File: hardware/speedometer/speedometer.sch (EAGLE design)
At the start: 128 parts, among them IC1 PIC32MX274F256DT-I_PT, IC10 TPS63001DRCT, IC11 TPS63002DRCT, IC2 CSTCE8M00G55-R0, IC3 HM-11, IC4 BQ27441DRZR-G1A, IC5 BQ24075RGTT, IC6 NRF24L01P-T, IC7 CSTCE16M0V53-R0, IC8 24LC024SN, IC9 MAX16054AZT+T, J1 10104111-0001LF, J2 BAT, J3 CONUFL001-SMD-T, J4 Right_sens, J5 Right, J6 Left_sens, J7 Left, Q1 BC817, Q2 BC817, Q3 BC817, Q4 BC817, U1 SN74AHC1G08DBVR, U2 SN74AHC1G08DBVR

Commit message: wip, mostly done
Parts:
- removed JP1, JP2: (no value), pinhead:PINHD-1X2
- added X1, X2: TSW-102-07-G-S, con-samtec:TSW-102-07-G-S
- SV1: device con-lsta:FE06-1 -> con-lstb:MA03-2
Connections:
- net +3V3: now also X2-1.1; no longer JP2.1
- net BL_TRIG: now also X2-2.1; no longer JP2.2
- net GND: now also X1-2.1; no longer JP1.2
- net N$41: now also X1-1.1; no longer JP1.1

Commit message: power added
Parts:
- C10, C21, C22, C25, C26, C27, C28: device rcl:C-EUC0603K -> rcl:C-EUC0805K
- C11: value 100n -> 10u; device rcl:C-EUC0603K -> rcl:C-EUC0805K
- C12: value 4u7 -> 10u; device rcl:CPOL-EUSMCA -> rcl:C-EUC0805K
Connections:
- net BQ_1V8: no longer R12.1
- net GND: now also C12.2, R12.1; no longer C12.-
- net VCCINT: now also C12.1; no longer C12.+
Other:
- moved on the sheet: C8, J2

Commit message: wip
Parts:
- C3: device rcl:C-EUC0603K -> rcl:C-EUC0805K
- SV1: device con-lstb:MA03-2 -> con-lstb:MA06-1
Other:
- moved on the sheet: SV1
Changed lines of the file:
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@@
 <part name="GND11" library="supply1" library_urn="urn:adsk.eagle:library:371" deviceset="GND" device=""/>
 <part name="VDD1" library="supply1" library_urn="urn:adsk.eagle:library:371" deviceset="VDD" device=""/>
-<part name="C3" library="rcl" library_urn="urn:adsk.eagle:library:334" deviceset="C-EU" device="C0603K" value="10u"/>
+<part name="C3" library="rcl" library_urn="urn:adsk.eagle:library:334" deviceset="C-EU" device="C0805K" package3d_urn="urn:adsk.eagle:package:23681/2" value="10u"/>
 <part name="GND2" library="supply1" library_urn="urn:adsk.eagle:library:371" deviceset="GND" device=""/>
 <part name="C1" library="rcl" library_urn="urn:adsk.eagle:library:334" deviceset="C-EU" device="C0603K" value="100n"/>
@@
 <part name="GND63" library="supply1" library_urn="urn:adsk.eagle:library:371" deviceset="GND" device=""/>
 <part name="+3V2" library="supply1" library_urn="urn:adsk.eagle:library:371" deviceset="+3V3" device=""/>
-<part name="SV1" library="con-lstb" library_urn="urn:adsk.eagle:library:162" deviceset="MA03-2" device="" package3d_urn="urn:adsk.eagle:package:8334/1"/>
 <part name="X1" library="con-samtec" library_urn="urn:adsk.eagle:library:184" deviceset="TSW-102-*-G-S" device="" technology="07"/>
 <part name="X2" library="con-samtec" library_urn="urn:adsk.eagle:library:184" deviceset="TSW-102-*-G-S" device="" technology="07"/>
 <part name="GND64" library="supply1" library_urn="urn:adsk.eagle:library:371" deviceset="GND" device=""/>
+<part name="SV1" library="con-lstb" library_urn="urn:adsk.eagle:library:162" deviceset="MA06-1" device="" package3d_urn="urn:adsk.eagle:package:8340/1"/>
 </parts>
 <sheets>
@@
 <attribute name="SHEET" x="230.505" y="5.08" size="2.54" layer="94"/>
 </instance>
-<instance part="GND1" gate="1" x="40.64" y="149.86" smashed="yes">
-<attribute name="VALUE" x="38.1" y="147.32" size="1.778" layer="96"/>
-</instance>
-<instance part="+3V34" gate="G$1" x="7.62" y="167.64" smashed="yes" rot="R90">
-<attribute name="VALUE" x="12.7" y="165.1" size="1.778" layer="96" rot="R180"/>
+<instance part="GND1" gate="1" x="27.94" y="149.86" smashed="yes">
+<attribute name="VALUE" x="25.4" y="147.32" size="1.778" layer="96"/>
+</instance>
+<instance part="+3V34" gate="G$1" x="50.8" y="165.1" smashed="yes" rot="R270">
+<attribute name="VALUE" x="45.72" y="167.64" size="1.778" layer="96"/>
 </instance>
 <instance part="TP8" gate="G$1" x="236.22" y="139.7" smashed="yes">
@@
 <attribute name="VALUE" x="34.29" y="50.038" size="1.778" layer="96"/>
 </instance>
-<instance part="SV1" gate="1" x="30.48" y="160.02" smashed="yes" rot="MR180">
-<attribute name="VALUE" x="26.67" y="167.64" size="1.778" layer="96" rot="MR180"/>
-<attribute name="NAME" x="26.67" y="154.178" size="1.778" layer="95" rot="MR180"/>
-</instance>
 <instance part="X1" gate="-1" x="95.25" y="142.24" smashed="yes">
 <attribute name="VALUE" x="93.98" y="143.51" size="1.778" layer="96"/>
@@
 <instance part="X2" gate="-2" x="110.49" y="27.94" smashed="yes">
 <attribute name="NAME" x="113.03" y="27.178" size="1.524" layer="95"/>
+</instance>
+<instance part="SV1" gate="1" x="15.24" y="160.02" smashed="yes" rot="MR180">
+<attribute name="VALUE" x="13.97" y="172.72" size="1.778" layer="96" rot="MR180"/>
+<attribute name="NAME" x="13.97" y="151.638" size="1.778" layer="95" rot="MR180"/>
 </instance>
 </instances>
@@
 <segment>
 <pinref part="SV1" gate="1" pin="3"/>
-<wire x1="38.1" y1="160.02" x2="40.64" y2="160.02" width="0.1524" layer="91"/>
+<wire x1="22.86" y1="162.56" x2="27.94" y2="162.56" width="0.1524" layer="91"/>
 <pinref part="GND1" gate="1" pin="GND"/>
-<wire x1="40.64" y1="160.02" x2="40.64" y2="152.4" width="0.1524" layer="91"/>
+<wire x1="27.94" y1="162.56" x2="27.94" y2="152.4" width="0.1524" layer="91"/>
 </segment>
 </net>
@@
 </segment>
 <segment>
+<pinref part="SV1" gate="1" pin="2"/>
 <pinref part="+3V34" gate="G$1" pin="+3V3"/>
-<wire x1="10.16" y1="167.64" x2="15.24" y2="167.64" width="0.1524" layer="91"/>
-<wire x1="15.24" y1="167.64" x2="15.24" y2="162.56" width="0.1524" layer="91"/>
-<pinref part="SV1" gate="1" pin="2"/>
-<wire x1="15.24" y1="162.56" x2="22.86" y2="162.56" width="0.1524" layer="91"/>
+<wire x1="22.86" y1="165.1" x2="48.26" y2="165.1" width="0.1524" layer="91"/>
 </segment>
 </net>
@@
 <segment>
 <pinref part="SV1" gate="1" pin="5"/>
-<wire x1="38.1" y1="157.48" x2="45.72" y2="157.48" width="0.1524" layer="91"/>
-<label x="45.72" y="157.48" size="1.27" layer="95" font="vector" xref="yes"/>
+<wire x1="22.86" y1="157.48" x2="33.02" y2="157.48" width="0.1524" layer="91"/>
+<wire x1="33.02" y1="157.48" x2="33.02" y2="154.94" width="0.1524" layer="91"/>
+<wire x1="33.02" y1="154.94" x2="35.56" y2="154.94" width="0.1524" layer="91"/>
+<label x="35.56" y="154.94" size="1.778" layer="95" font="vector" xref="yes"/>
 </segment>
 </net>
@@
 <segment>
 <pinref part="SV1" gate="1" pin="4"/>
-<wire x1="22.86" y1="160.02" x2="15.24" y2="160.02" width="0.1524" layer="91"/>
-<label x="15.24" y="160.02" size="1.27" layer="95" font="vector" rot="R180" xref="yes"/>
+<wire x1="22.86" y1="160.02" x2="35.56" y2="160.02" width="0.1524" layer="91"/>
+<label x="35.56" y="160.02" size="1.778" layer="95" font="vector" xref="yes"/>
 </segment>
 </net>
@@
 <segment>
 <pinref part="SV1" gate="1" pin="1"/>
-<wire x1="38.1" y1="162.56" x2="45.72" y2="162.56" width="0.1524" layer="91"/>
-<label x="45.72" y="162.56" size="1.27" layer="95" font="vector" xref="yes"/>
-</segment>
-</net>
+<wire x1="22.86" y1="167.64" x2="35.56" y2="167.64" width="0.1524" layer="91"/>
+<label x="35.56" y="167.64" size="1.778" layer="95" font="vector" xref="yes"/>
+</segment>
+</net>

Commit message: wip
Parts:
- added IC12: SN65220DBVRG4, SN65220DBVRG4:SN65220DBVRG4
- IC8: value 24LC024SN -> 24LC024ST; device microchip:24LC024SN -> microchip:24LC024ST
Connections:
- net GND: now also IC12.GND
- net USB_D+: now also IC12.A
- net USB_D-: now also IC12.B
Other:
- moved on the sheet: C6, J1, R2, R3, TP1, TP2, X1-1, X1-2

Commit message: wip
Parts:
- added C30, C31, C32: (no value), rcl:C-EUC0402K
- added R36, R37, R38: 0, rcl:R-US_R0402
- added U$1: M310210, m310210:M310210
- C18: value 1p5 -> (none)
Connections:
- new net N$17: C19.1, L2.P$1, R36.2
- new net N$20: C18.2, C30.1, R37.1, R38.1
- new net N$23: J3.SIG, R37.2
- new net N$36: C32.1, U$1.GND
- net GND: now also C30.2, C31.2, C32.2
- net N$32: now also R36.1; no longer L2.P$1
- net N$37: now also C31.1, R38.2, U$1.FEED; no longer C18.2, C19.1, J3.SIG
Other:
- moved on the sheet: C15, C16, C17, C18, C19, IC6, IC7, J3, L1, L2, L3, R19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

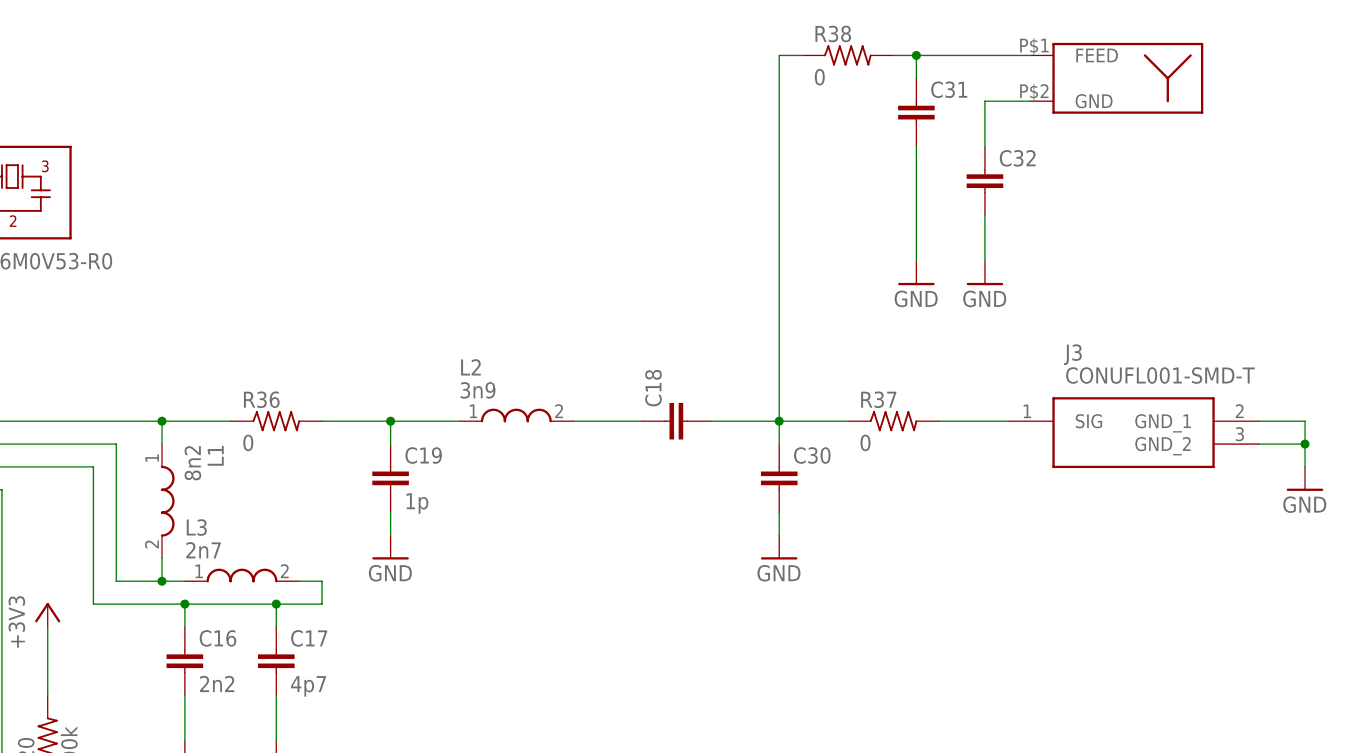
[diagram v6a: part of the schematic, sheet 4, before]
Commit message: aligned with GF suggestion, waiting approval
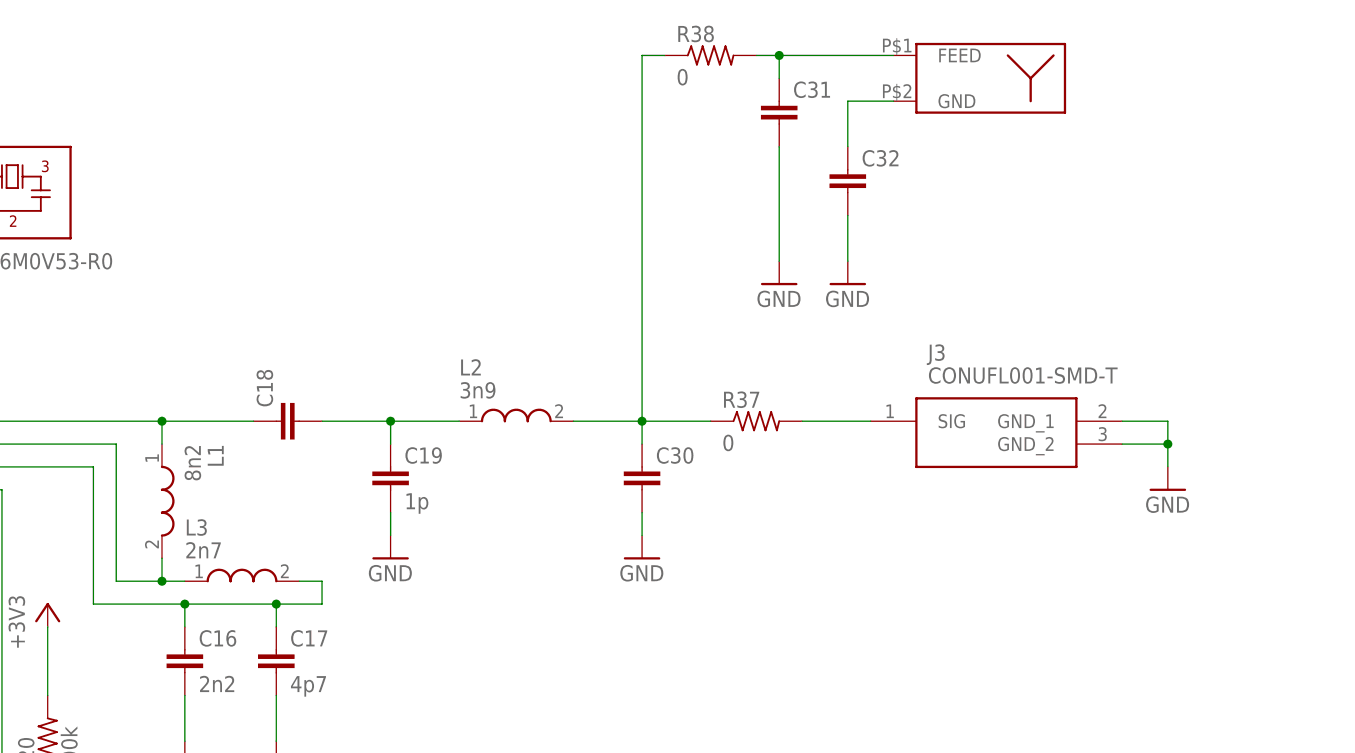
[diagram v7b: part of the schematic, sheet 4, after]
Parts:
- removed R10: 470, rcl:R-US_R0603
- removed R36: 0, rcl:R-US_R0402
- added TP25, TP26: TPB1,27, testpad:TPB1,27
- added U$2: 74LVC1G32SE-7, 74LVC1G32SE:74LVC1G32SE-7
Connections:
- removed net BT_KEY: IC1.RPC5/PMD7/RC5, R10.2
- removed net N$18: C18.1, L2.P$2
- new net KEEP_SYS_EN: IC1.RPC5/PMD7/RC5, TP26.TP, U$2.B
- new net MAX_SYS_ON: IC9.OUT, TP25.TP, U$2.A
- net GND: now also U$2.GND
- net N$17: now also C18.2; no longer R36.2
- net N$2: no longer R10.1
- net N$20: now also L2.P$2; no longer C18.2
- net N$32: now also C18.1; no longer R36.1
- net SYS_EN: now also U$2.Y; no longer IC9.OUT
- net VCCINT: now also U$2.VCC
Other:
- moved on the sheet: C18, C30, C31, C32, IC9, J3, R37, R38, S1, TP20

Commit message: part renumber
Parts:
- removed CHG, STATUS: (no value), led:LED3MM
- removed R37, R38: 0, rcl:R-US_R0402
- added LED5, LED6: (no value), led:LEDCHIPLED_1206
- added R10: 470, rcl:R-US_R0603
- added R36: 1k5, rcl:R-US_R0603
- C15: value 33n -> 1n; device rcl:C-EUC0402K -> rcl:C-EUC0603K
- C16: value 2n2 -> 33n
- C17: value 4p7 -> 2n2
- C19: value 1p -> 4p7
- C20: value 100n -> 1p; device rcl:C-EUC0603K -> rcl:C-EUC0402K
- C21, C22: value 10u -> (none); device rcl:C-EUC0805K -> rcl:C-EUC0402K
- C23: value 100n -> (none); device rcl:C-EUC0603K -> rcl:C-EUC0402K
- C27, C28: value 10u -> 100n; device rcl:C-EUC0805K -> rcl:C-EUC0603K
- C29: value 1n -> 10u; device rcl:C-EUC0603K -> rcl:C-EUC0805K
- C30, C31, C32: value (none) -> 10u; device rcl:C-EUC0402K -> rcl:C-EUC0805K
- IC10: value TPS63001DRCT -> MAX16054AZT+T; device TPS63000DRCT:TPS63000DRCT -> MAX16054AZT+T:MAX16054AZT+T
- IC11: value TPS63002DRCT -> TPS63001DRCT
- IC12: value SN65220DBVRG4 -> TPS63002DRCT; device SN65220DBVRG4:SN65220DBVRG4 -> TPS63000DRCT:TPS63000DRCT
- IC2: value CSTCE8M00G55-R0 -> SN65220DBVRG4; device CSTCE12M0G15L99-R0:CSTCE12M0G15L99-R0 -> SN65220DBVRG4:SN65220DBVRG4
- IC3: value HM-11 -> CSTCE8M00G55-R0; device HM11:HM-11 -> CSTCE12M0G15L99-R0:CSTCE12M0G15L99-R0
- IC4: value BQ27441DRZR-G1A -> HM-11; device BQ27441DRZR-G1A:BQ27441DRZR-G1A -> HM11:HM-11
- IC5: value BQ24075RGTT -> BQ27441DRZR-G1A; device BQ24075RGTT:BQ24075RGTT -> BQ27441DRZR-G1A:BQ27441DRZR-G1A
- IC6: value NRF24L01P-T -> BQ24075RGTT; device nRF24L01P-T:NRF24L01P-T -> BQ24075RGTT:BQ24075RGTT
- IC7: value CSTCE16M0V53-R0 -> NRF24L01P-T; device CSTCE12M0G15L99-R0:CSTCE12M0G15L99-R0 -> nRF24L01P-T:NRF24L01P-T
- IC8: value 24LC024ST -> CSTCE16M0V53-R0; device microchip:24LC024ST -> CSTCE12M0G15L99-R0:CSTCE12M0G15L99-R0
- IC9: value MAX16054AZT+T -> 24LC024ST; device MAX16054AZT+T:MAX16054AZT+T -> microchip:24LC024ST
- L2: value 3n9 -> 2n7
- L3: value 2n7 -> 3n9
- LED1: device led:LEDCHIPLED_0805 -> led:LED3MM
- LED2: device led:LEDCHIPLED_1206 -> led:LEDCHIPLED_0805
- LED4: device led:LEDCHIPLED_1206 -> led:LED3MM
- R2: value 1k -> 1k5
- R21, R22: value 100 -> 0; device rcl:R-US_R0603 -> rcl:R-US_R0402; RS_PART_NUMBER 740-8978 -> (none)
- R23, R24: value 10k -> 100; RS_PART_NUMBER (none) -> 740-8978
- R25: value 100k -> 10k
- R28, R32, R35: value 1k5 -> 10k
- R29, R34: value 10k -> 100k
- R3: value 10k -> 1k
- R30: value 100k -> 1k5
- R5: value 4k7 -> 10k
- R8: value 470 -> 4k7
- TP20: TP_SIGNAL_NAME TP_SYS_EN -> TP_SYS_EN_PIC
- TP21: TP_SIGNAL_NAME TP_3V3 -> TP_SYS_EN_MAX
- TP22: TP_SIGNAL_NAME TP_5V -> TP_3V3
- TP23: TP_SIGNAL_NAME TP_L_DX -> TP_5V
- TP24: TP_SIGNAL_NAME TP_L_DX -> TP_SYS_EN
- TP25: TP_SIGNAL_NAME TP_SYS_EN_MAX -> TP_L_DX
- TP26: TP_SIGNAL_NAME TP_SYS_EN_PIC -> TP_L_DX
- renumbered BT to LED3, JP3 to JP1, U$1 to ANT1, U$2 to IC13
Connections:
- removed net N$10 (its old number): R35.1, STATUS.C
- new net N$29: LED2.C, R2.1
- net !BAT_CHG: now also IC6.!CHG, LED4.C; no longer CHG.C, IC5.!CHG
- net !MCLR: now also R3.1; no longer R2.1
- net +3V3: now also C15.1, C24.1, C31.1, IC11.FB, IC11.VOUT, IC4.VCC, IC6.EN1, IC7.VDD_1, IC7.VDD_2, IC7.VDD_3, IC9.VCC, R28.2, R35.2, R4.2, R8.2, TP22.TP; no longer C20.1, C25.1, C27.1, IC10.FB, IC10.VOUT, IC3.VCC, IC5.EN1, IC6.VDD_1, IC6.VDD_2, IC6.VDD_3, IC8.VCC, R26.2, R3.2, R34.2, R5.2, TP21.TP
- net +5V: now also C30.1, C32.1, IC12.FB, IC12.VOUT, LED5.A, LED6.A, TP23.TP; no longer C26.1, C28.1, IC11.FB, IC11.VOUT, LED2.A, LED4.A, TP22.TP
- net BL_TRIG: now also R5.2; no longer R4.2
- net BQ_1V8: now also IC5.VDD; no longer IC4.VDD
- net BQ_PGOOD: now also IC6.!PGOOD; no longer IC5.!PGOOD
- net BT_RST: now also R9.1; no longer R7.1
- net GAUGE_GP: now also IC5.GPOUT; no longer IC4.GPOUT
- net GND: now also IC10.CLEAR, IC12.PGND, IC2.GND, IC3.2, IC4.GND, IC5.EP, IC6.!CE, IC6.EN2, IC6.SYSOFF, IC6.VSS, IC6.VSS_TP, IC7.TP_GND, IC7.VSS_1, IC7.VSS_2, IC7.VSS_3, IC7.VSS_4, IC8.2, IC9.A0, IC9.A1, IC9.A2, IC9.WP, R2.2, R29.2, R34.2, R5.1; no longer IC10.PGND, IC2.2, IC3.GND, IC4.EP, IC4.VSS, IC5.!CE, IC5.EN2, IC5.SYSOFF, IC5.VSS_TP, IC6.TP_GND, IC6.VSS_1, IC6.VSS_2, IC6.VSS_3, IC6.VSS_4, IC7.2, IC8.A0, IC8.A1, IC8.A2, IC8.GND, IC8.WP, IC9.CLEAR, R25.2, R30.2, R35.2, R4.1
- net I2C2_SCL: now also IC5.SCL, IC9.SCL, R7.1; no longer IC4.SCL, IC8.SCL, R6.1
- net I2C2_SDA: now also IC5.SDA, IC9.SDA, R6.1; no longer IC4.SDA, IC8.SDA, R5.1
- net IN_L: now also R35.1; no longer R34.1
- net IN_R: now also R28.1; no longer R26.1
- net KEEP_SYS_EN: now also TP20.TP; no longer TP26.TP
- net LED_HB: now also LED2.A; no longer LED1.A
- net LED_STS: now also LED1.A; no longer STATUS.A
- net MAX_SYS_ON: now also IC10.OUT, TP21.TP; no longer IC9.OUT, TP25.TP
- net N$1: now also IC4.!RESET, R9.2; no longer IC3.!RESET, R8.2
- net N$11: now also IC3.1; no longer IC2.1
- net N$12: now also LED4.A; no longer CHG.A
- net N$13: now also R32.2, R34.1; no longer R31.2, R33.1
- net N$14: now also R31.2, R33.1, TP26.TP; no longer R29.2, R30.1, TP24.TP
- net N$15: now also LED6.C, R36.2; no longer LED2.C, R32.2
- net N$16: now also R31.1; no longer R29.1
- net N$17: now also C20.1, L3.P$1; no longer C19.1, L2.P$1
- net N$19: now also IC3.3; no longer IC2.3
- net N$2: now also IC4.PIO0/KEY; no longer IC3.PIO0/KEY
- net N$20: now also C21.1, L3.P$2, R21.1, R22.1; no longer C30.1, L2.P$2, R37.1, R38.1
- net N$22: now also IC7.XC2, IC8.1; no longer IC6.XC2, IC7.1
- net N$23: now also R22.2; no longer R37.2
- net N$24: now also IC7.IREF; no longer IC6.IREF
- net N$25: now also C16.1, IC7.DVDD; no longer C15.1, IC6.DVDD
- net N$26: now also R25.2, R27.1; no longer R23.2, R25.1
- net N$27: now also R25.1; no longer R23.1
- net N$28: now also R32.1; no longer R31.1
- net N$3: now also R36.1; no longer R32.1
- net N$30: now also IC5.BIN; no longer IC4.BIN
- net N$31: now also IC7.XC1, IC8.3; no longer IC6.XC1, IC7.3
- net N$32: now also IC7.ANT2; no longer IC6.ANT2
- net N$33: now also IC7.ANT1, L2.P$1; no longer IC6.ANT1, L3.P$1
- net N$34: now also IC11.L2; no longer IC10.L2
- net N$35: now also C19.1, IC7.VDD_PA, L2.P$2; no longer C16.1, IC6.VDD_PA, L3.P$2
- net N$36: now also C23.1; no longer C32.1
- net N$37: now also C22.1, R21.2; no longer C31.1, R38.2
- net N$38: now also R30.1; no longer R28.1
- net N$39: now also R26.2, R29.1, TP25.TP; no longer R24.2, R27.1, TP23.TP
- net N$4: now also IC4.PIO1/LED, R10.1; no longer IC3.PIO1/LED, R9.1
- net N$40: now also LED5.C, R30.2; no longer LED4.C, R28.2
- net N$41: now also R3.2, R4.1; no longer R2.2, R3.1
- net N$42: now also R26.1; no longer R24.1
- net N$5: now also IC11.L1; no longer IC10.L1
- net N$58: now also IC10.IN; no longer IC9.IN
- net N$59: now also IC12.L1; no longer IC11.L1
- net N$6: now also R10.2; no longer R9.2
- net N$60: now also C27.1, IC11.PS/SYNC, IC11.VINA, R23.1; no longer C23.1, IC10.PS/SYNC, IC10.VINA, R21.1
- net N$61: now also IC12.L2; no longer IC11.L2
- net N$62: now also C28.1, IC12.PS/SYNC, IC12.VINA, R24.1; no longer C24.1, IC11.PS/SYNC, IC11.VINA, R22.1
- net N$7: now also IC6.TS; no longer IC5.TS
- net N$8: now also IC6.ILIM; no longer IC5.ILIM
- net N$9: now also IC6.ISET; no longer IC5.ISET
- net NRF_!CS: now also IC7.CSN; no longer IC6.CSN
- net NRF_CE: now also IC7.CE; no longer IC6.CE
- net NRF_IRQ: now also IC7.IRQ; no longer IC6.IRQ
- net SPI1_SCK: now also IC7.SCK; no longer IC6.SCK
- net SPI1_SDI: now also IC7.MISO; no longer IC6.MISO
- net SPI1_SDO: now also IC7.MOSI; no longer IC6.MOSI
- net SYS_EN: now also IC12.EN, TP24.TP; no longer IC10.EN, TP20.TP
- net U1_RX: now also IC4.UART_TX; no longer IC3.UART_TX
- net U1_TX: now also IC4.UART_RX; no longer IC3.UART_RX
- net USB_D+: now also IC2.A; no longer IC12.A
- net USB_D-: now also IC2.B; no longer IC12.B
- net VBAT: now also IC5.SRN, IC6.BAT_1, IC6.BAT_2; no longer IC4.SRN, IC5.BAT_1, IC5.BAT_2
- net VCCINT: now also C25.1, C26.1, IC10.VCC, IC12.VIN, IC6.OUT_1, IC6.OUT_2, R23.2, R24.2; no longer C21.1, C22.1, IC10.VIN, IC5.OUT_1, IC5.OUT_2, IC9.VCC, R21.2, R22.2
- net VDD: now also IC6.IN; no longer IC5.IN
- net _VBAT: now also IC5.BAT, IC5.SRP; no longer IC4.BAT, IC4.SRP
